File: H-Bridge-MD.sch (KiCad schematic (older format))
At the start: 80 parts, among them IC1 SI8650AB-B-IS1, IC2 A3921KLPTR-T, IC3 SI8650AB-B-IS1, IC4 A3921KLPTR-T, J1 PRT-10474, J2 Conn_01x02, J3 Conn_01x05, J4 PRT-10474, J5 Bus_PCIexpress_x16_164_Positi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, Q1 NVMFD5C650NLWFT1G, Q2 NVMFD5C650NLWFT1G, Q3 NVMFD5C650NLWFT1G, Q4 NVMFD5C650NLWFT1G, SW1 SW_Push, U1 LDO_3.3V, U2 STM32F042K6Tx, U3 MCP2562-E-SN

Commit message: Prototype1.2
Change: ST-LINK Conn, Rgs, Rg
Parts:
- removed R14, R15, R18, R19, R22, R23, R7, R8: 10K, Resistor_SMD:R_0603_1608Metric, symbol Device:R
- D6, D7: footprint Diode_SMD:D_2010_5025Metric -> Diode_SMD:D_0603_1608Metric
- R12, R13, R16, R17, R20, R21, R4, R5: value 100 -> 21
- R24, R27: value 30K -> 3K
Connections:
- wire segments 335 -> 295
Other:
- moved on the sheet: R12, R13, R16, R17, R20, R21, R4, R5

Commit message: Prototype1.3
Change LDO, 0.47uF size
Correction ST-LINK foot-print
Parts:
- removed U1: LDO_3.3V, Package_TO_SOT_SMD:TO-252-2, symbol Regulator_Linear:LF33_TO252
- added U1: LDL1117S33TR_SOT223-4, Package_TO_SOT_SMD:SOT-223-3_TabPin2, symbol Regulator_Linear:LD1117S33TR_SOT223
- C1: value 0.1uF -> 1uF
- C11, C17: footprint Capacitor_SMD:C_1206_3216Metric -> Capacitor_SMD:C_0805_2012Metric
- C2: value 0.1uF -> 4.7uF
- D1, D10, D11, D2, D3, D4, D5, D8, D9: footprint Diode_SMD:D_0603_1608Metric -> LED_SMD:LED_0603_1608Metric
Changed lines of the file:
@@
 Text GLabel 6050 7650 2    50   Output ~ 0
 MD_PWMH_1
-$Comp
-L Regulator_Linear:LF33_TO252 U1
-U 1 1 5DABB8B6
-P 1350 1650
-F 0 "U1" H 1200 1775 50  0000 C CNN
-F 1 "LDO_3.3V " H 1350 1775 50  0000 L CNN
-F 2 "Package_TO_SOT_SMD:TO-252-2" H 1350 1875 50  0001 C CIN
-F 3 "http://www.st.com/content/ccc/resource/technical/document/datasheet/c4/0e/7e/2a/be/bc/4c/bd/CD00000546.pdf/files/CD00000546.pdf/jcr:content/translations/en.CD00000546.pdf" H 1350 1600 50  0001 C CNN
-	1    1350 1650
-	1    0    0    -1
-$EndComp
 Wire Wire Line
 	7350 10500 7700 10500
@@
 P 1000 1800
 F 0 "C1" V 748 1800 50  0000 C CNN
-F 1 "0.1uF" V 839 1800 50  0000 C CNN
+F 1 "1uF" V 839 1800 50  0000 C CNN
 F 2 "Capacitor_SMD:C_0805_2012Metric" H 1038 1650 50  0001 C CNN
 F 3 "~" H 1000 1800 50  0001 C CNN
@@
 P 1700 1800
 F 0 "C2" V 1448 1800 50  0000 C CNN
-F 1 "0.1uF" V 1539 1800 50  0000 C CNN
+F 1 "4.7uF" V 1539 1800 50  0000 C CNN
 F 2 "Capacitor_SMD:C_0805_2012Metric" H 1738 1650 50  0001 C CNN
 F 3 "~" H 1700 1800 50  0001 C CNN
@@
 F 0 "D3" V 1339 2962 50  0000 C CNN
 F 1 "LED" V 1248 2962 50  0000 C CNN
-F 2 "Diode_SMD:D_0603_1608Metric" H 1300 3150 50  0001 C CNN
+F 2 "LED_SMD:LED_0603_1608Metric" H 1300 3150 50  0001 C CNN
 F 3 "~" H 1300 3150 50  0001 C CNN
 	1    1300 3150
@@
 F 0 "D2" V 1039 2962 50  0000 C CNN
 F 1 "LED" V 948 2962 50  0000 C CNN
-F 2 "Diode_SMD:D_0603_1608Metric" H 1000 3150 50  0001 C CNN
+F 2 "LED_SMD:LED_0603_1608Metric" H 1000 3150 50  0001 C CNN
 F 3 "~" H 1000 3150 50  0001 C CNN
 	1    1000 3150
@@
 F 0 "D1" V 739 3300 50  0000 C CNN
 F 1 "LED" V 648 3300 50  0000 C CNN
-F 2 "Diode_SMD:D_0603_1608Metric" H 700 3150 50  0001 C CNN
+F 2 "LED_SMD:LED_0603_1608Metric" H 700 3150 50  0001 C CNN
 F 3 "~" H 700 3150 50  0001 C CNN
 	1    700  3150
@@
 U 1 1 5E29BEB6
 P 7050 10250
-F 0 "C9" H 7165 10296 50  0000 L CNN
-F 1 "0.1uF" H 7165 10205 50  0000 L CNN
+F 0 "C9" H 7164 10204 50  0000 L CNN
+F 1 "0.1uF" H 7164 10295 50  0000 L CNN
 F 2 "Capacitor_SMD:C_0805_2012Metric" H 7088 10100 50  0001 C CNN
 F 3 "~" H 7050 10250 50  0001 C CNN
 	1    7050 10250
-	1    0    0    -1
+	-1   0    0    1
 $EndComp
 $Comp
@@
 U 1 1 5E2AD1D6
 P 7050 9750
-F 0 "C8" H 7165 9796 50  0000 L CNN
-F 1 "0.1uF" H 7165 9705 50  0000 L CNN
+F 0 "C8" H 6723 9796 50  0000 L CNN
+F 1 "0.1uF" H 6723 9705 50  0000 L CNN
 F 2 "Capacitor_SMD:C_0805_2012Metric" H 7088 9600 50  0001 C CNN
 F 3 "~" H 7050 9750 50  0001 C CNN
@@
 U 1 1 5E35AA28
 P 11250 6200
-F 0 "C14" H 11365 6246 50  0000 L CNN
-F 1 "0.1uF" H 11365 6155 50  0000 L CNN
+F 0 "C14" H 10923 6246 50  0000 L CNN
+F 1 "0.1uF" H 10923 6155 50  0000 L CNN
 F 2 "Capacitor_SMD:C_0805_2012Metric" H 11288 6050 50  0001 C CNN
 F 3 "~" H 11250 6200 50  0001 C CNN
@@
 U 1 1 5E36BC53
 P 11250 6700
-F 0 "C15" H 11365 6746 50  0000 L CNN
-F 1 "0.1uF" H 11365 6655 50  0000 L CNN
+F 0 "C15" H 10923 6746 50  0000 L CNN
+F 1 "0.1uF" H 10923 6655 50  0000 L CNN
 F 2 "Capacitor_SMD:C_0805_2012Metric" H 11288 6550 50  0001 C CNN
 F 3 "~" H 11250 6700 50  0001 C CNN
@@
 F 0 "C17" H 13174 7054 50  0000 L CNN
 F 1 "0.47uF" H 13174 7145 50  0000 L CNN
-F 2 "Capacitor_SMD:C_1206_3216Metric" H 13588 6950 50  0001 C CNN
+F 2 "Capacitor_SMD:C_0805_2012Metric" H 13588 6950 50  0001 C CNN
 F 3 "~" H 13550 7100 50  0001 C CNN
 	1    13550 7100
@@
 F 0 "C11" H 9465 10696 50  0000 L CNN
 F 1 "0.47uF" H 9465 10605 50  0000 L CNN
-F 2 "Capacitor_SMD:C_1206_3216Metric" H 9388 10500 50  0001 C CNN
+F 2 "Capacitor_SMD:C_0805_2012Metric" H 9388 10500 50  0001 C CNN
 F 3 "~" H 9350 10650 50  0001 C CNN
 	1    9350 10650
@@
 F 0 "D4" V 1639 2962 50  0000 C CNN
 F 1 "LED" V 1548 2962 50  0000 C CNN
-F 2 "Diode_SMD:D_0603_1608Metric" H 1600 3150 50  0001 C CNN
+F 2 "LED_SMD:LED_0603_1608Metric" H 1600 3150 50  0001 C CNN
 F 3 "~" H 1600 3150 50  0001 C CNN
 	1    1600 3150
@@
 F 0 "D5" V 2389 1033 50  0000 R CNN
 F 1 "LED" V 2298 1033 50  0000 R CNN
-F 2 "Diode_SMD:D_0603_1608Metric" H 2350 1150 50  0001 C CNN
+F 2 "LED_SMD:LED_0603_1608Metric" H 2350 1150 50  0001 C CNN
 F 3 "~" H 2350 1150 50  0001 C CNN
 	1    2350 1150
@@
 F 0 "D10" V 14239 8083 50  0000 R CNN
 F 1 "LED" V 14148 8083 50  0000 R CNN
-F 2 "Diode_SMD:D_0603_1608Metric" H 14200 8200 50  0001 C CNN
+F 2 "LED_SMD:LED_0603_1608Metric" H 14200 8200 50  0001 C CNN
 F 3 "~" H 14200 8200 50  0001 C CNN
 	1    14200 8200
@@
 F 0 "D11" V 14589 8083 50  0000 R CNN
 F 1 "LED" V 14498 8083 50  0000 R CNN
-F 2 "Diode_SMD:D_0603_1608Metric" H 14550 8200 50  0001 C CNN
+F 2 "LED_SMD:LED_0603_1608Metric" H 14550 8200 50  0001 C CNN
 F 3 "~" H 14550 8200 50  0001 C CNN
 	1    14550 8200
@@
 F 0 "D9" V 7989 8383 50  0000 R CNN
 F 1 "LED" V 7898 8383 50  0000 R CNN
-F 2 "Diode_SMD:D_0603_1608Metric" H 7950 8500 50  0001 C CNN
+F 2 "LED_SMD:LED_0603_1608Metric" H 7950 8500 50  0001 C CNN
 F 3 "~" H 7950 8500 50  0001 C CNN
 	1    7950 8500
@@
 F 0 "D8" V 7639 8383 50  0000 R CNN
 F 1 "LED" V 7548 8383 50  0000 R CNN
-F 2 "Diode_SMD:D_0603_1608Metric" H 7600 8500 50  0001 C CNN
+F 2 "LED_SMD:LED_0603_1608Metric" H 7600 8500 50  0001 C CNN
 F 3 "~" H 7600 8500 50  0001 C CNN
 	1    7600 8500
@@
 	4500 9700 4500 9500
 Connection ~ 4500 9500
+$Comp
+L Regulator_Linear:LD1117S33TR_SOT223 U1
+U 1 1 5DEBD597
+P 1350 1650
+F 0 "U1" H 1200 1775 50  0000 C CNN
+F 1 "LDL1117S33TR_SOT223-4" H 1350 1775 50  0000 L CNN
+F 2 "Package_TO_SOT_SMD:SOT-223-3_TabPin2" H 1350 1850 50  0001 C CNN
+F 3 "http://www.st.com/st-web-ui/static/active/en/resource/technical/document/datasheet/CD00000544.pdf" H 1450 1400 50  0001 C CNN
+	1    1350 1650
+	1    0    0    -1
+$EndComp
 $EndSCHEMATC

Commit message: update
軽微な配線の修正
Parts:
- removed J1, J4: PRT-10474, library:XT60PW-F_Reversible, symbol SamacSys_Parts:PRT-10474
- removed J2: Conn_01x02, Connector_JST:JST_XH_B2B-XH-A_1x02_P2.50mm_Vertical, symbol Connector_Generic:Conn_01x02
- removed J5: Bus_PCIexpress_x16_164_Position, library:BUS_PCIexpress_x16_164_Position, symbol SamacSys_Parts:Bus_PCIexpress_x16_164_Position
- removed R1, R2, R3, R6: 2.2K, Resistor_SMD:R_0603_1608Metric, symbol Device:R
- added J1, J4: Conn_01x02, XT60:XT60PW_Reversible, symbol Connector_Generic:Conn_01x02
- added J2: Conn_01x03, Connector_JST:JST_XH_B3B-XH-A_1x03_P2.50mm_Vertical, symbol Connector_Generic:Conn_01x03
- added J5: Bus_mechaken_PCIexpress_x16_164_Position, PCIe:BUS_mechaken_PCIexpress_x16_164_Position, symbol PCIe:Bus_mechaken_PCIexpress_x16_164_Position
- added RN1: R_Pack04, Resistor_SMD:R_Array_Concave_4x0603, symbol Device:R_Pack04
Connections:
- wire segments 295 -> 172
- no-connect marks 23 -> 15
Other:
- moved on the sheet: D1, D2, D3, D4

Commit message: remove RESET_SW
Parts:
- removed C3: 0.1uF, Capacitor_SMD:C_0805_2012Metric, symbol Device:C
- removed D5: LED, LED_SMD:LED_0603_1608Metric, symbol Device:LED
- removed Q1, Q2, Q3, Q4: NVMFD5C650NLWFT1G, SamacSys_Parts:NVMFD5C446NLWFT1G, symbol SamacSys_Parts:NVMFD5C650NLWFT1G
- removed R11, R9: 10K, Resistor_SMD:R_0603_1608Metric, symbol Device:R
- removed SW1: SW_Push, SamacSys_Parts:PTS647SM38SMTR2LFS, symbol Switch:SW_Push
- added Q1, Q2, Q3, Q4: NVMFD5C446NT1G, SamacSys_Parts:NVMFD5C446NLWFT1G, symbol SamacSys_Parts:NVMFD5C446NT1G
- J2: footprint Connector_JST:JST_XH_B3B-XH-A_1x03_P2.50mm_Vertical -> Connector_PinHeader_2.54mm:PinHeader_1x03_P2.54mm_Vertical
- J3: footprint Connector_JST:JST_XH_B5B-XH-A_1x05_P2.50mm_Vertical -> Connector_PinHeader_2.54mm:PinHeader_1x05_P2.54mm_Vertical
- U1: symbol Regulator_Linear:LD1117S33TR_SOT223 -> H-Bridge-MD-rescue:LD1117S33TR_SOT223-Regulator_Linear
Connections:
- net GNDPWR: now also Q2.1 (S1), Q2.3 (S2), Q3.1 (S1), Q3.3 (S2)
- net SA_0: now also Q3.6 (D1), Q4.1 (S1)
- net SA_1: now also Q1.1 (S1), Q2.6 (D1)
- net SB_0: now also Q3.5 (D2), Q4.3 (S2)
- net SB_1: now also Q1.3 (S2), Q2.5 (D2)
- net VCC: now also Q1.5 (D2), Q1.6 (D1), Q4.5 (D2), Q4.6 (D1)
- net at R12.2: now also Q2.2 (G1)
- net at R13.1: now also Q2.4 (G2)
- net at R4.2: now also Q1.2 (G1)
- net at R5.1: now also Q1.4 (G2)
- net at R16.2: now also Q3.2 (G1)
- net at R17.1: now also Q3.4 (G2)
- net at R20.2: now also Q4.2 (G1)
- net at R21.1: now also Q4.4 (G2)
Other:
- moved on the sheet: R20, R21

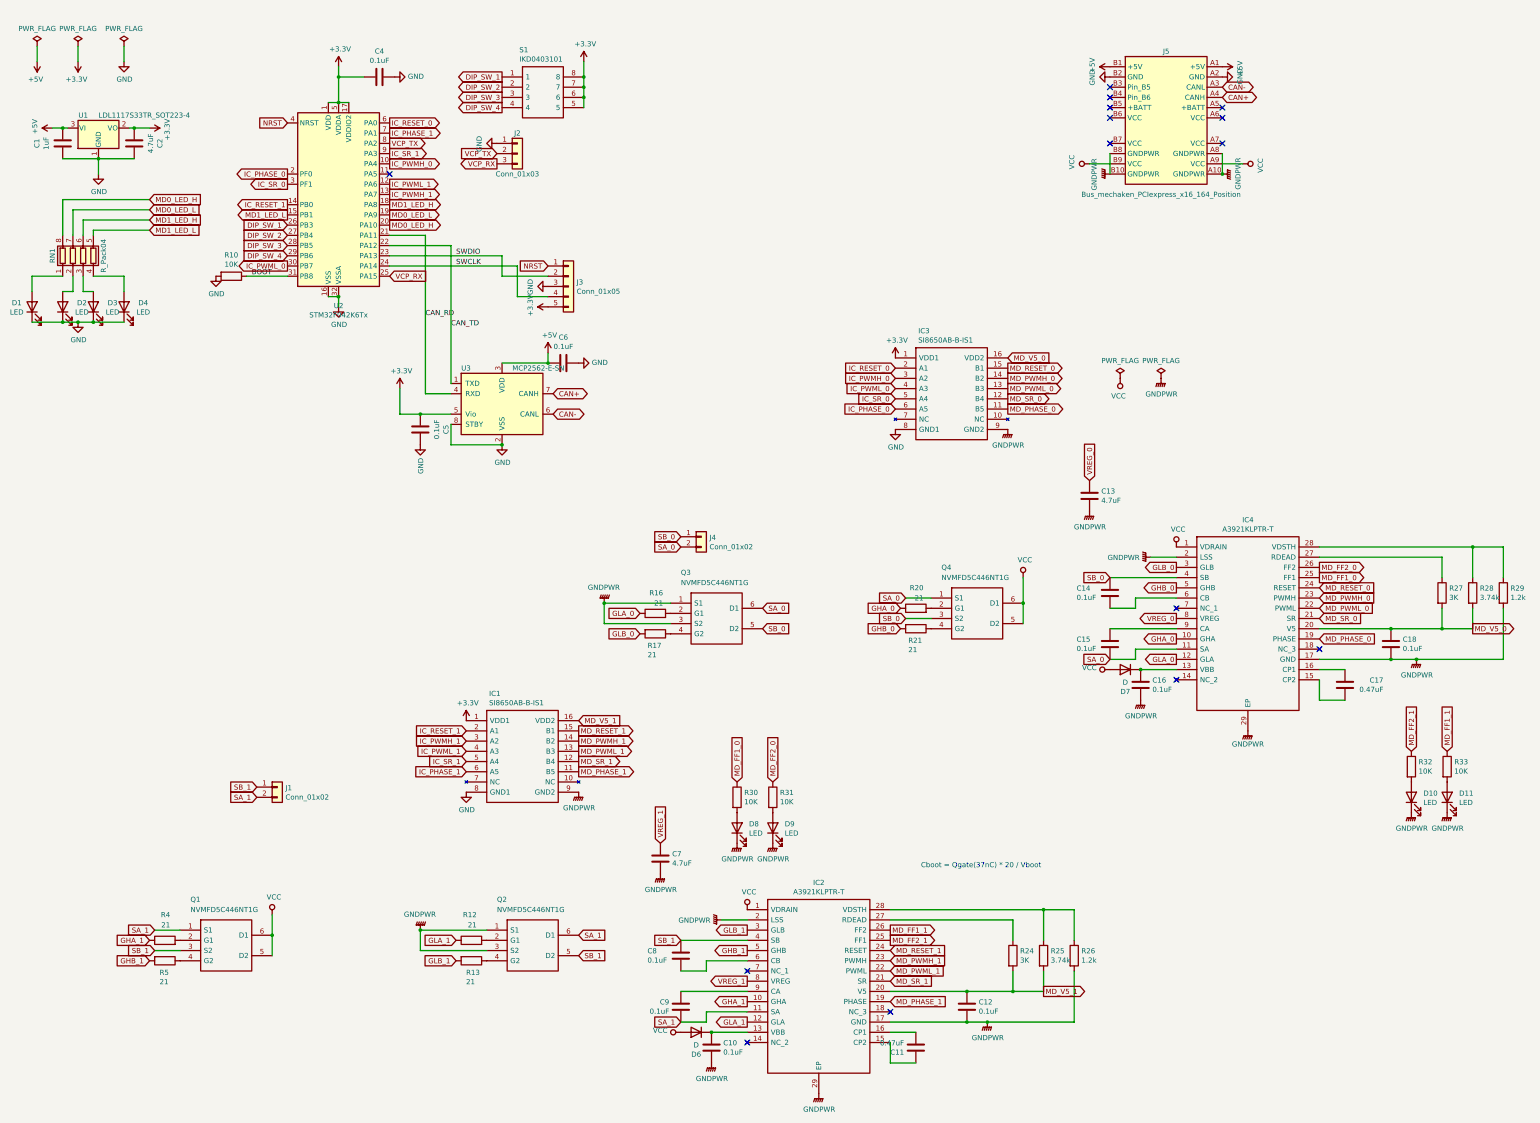
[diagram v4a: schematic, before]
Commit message: add 3V3LDO & pad
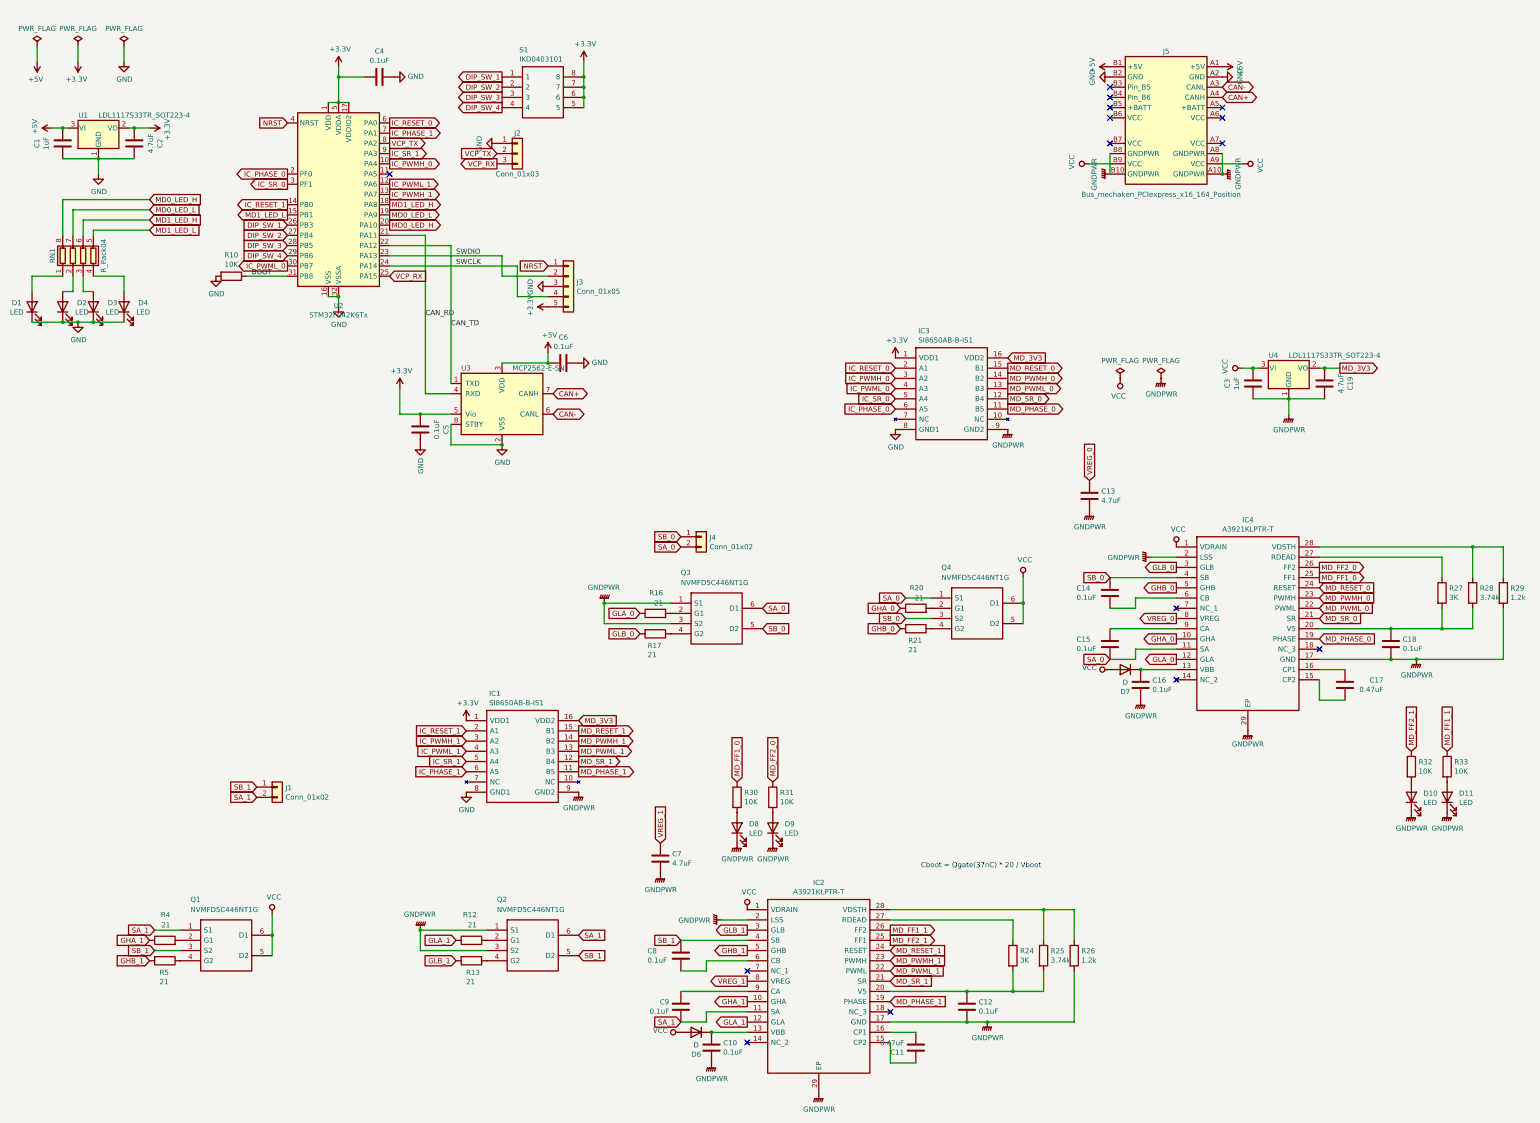
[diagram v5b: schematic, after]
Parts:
- added C19: 4.7uF, Capacitor_SMD:C_0805_2012Metric, symbol Device:C
- added C3: 1uF, Capacitor_SMD:C_0805_2012Metric, symbol Device:C
- added U4: LDL1117S33TR_SOT223-4, Package_TO_SOT_SMD:SOT-223-3_TabPin2, symbol H-Bridge-MD-rescue:LD1117S33TR_SOT223-Regulator_Linear
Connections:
- net GNDPWR: now also C19.1, C3.2, U4.1 (GND)
- net VCC: now also C3.1, U4.3 (VI)
- net MD_V5_0: no longer names the net of C18.1, IC4.20 (V5), R27.2, R28.2
- net MD_V5_0: no longer IC3.16 (VDD2)
- net MD_V5_1: no longer names the net of C12.1, IC2.20 (V5), R24.2, R25.2
- net MD_V5_1: no longer IC1.16 (VDD2)
- new net MD_3V3: C19.2, IC1.16 (VDD2), IC3.16 (VDD2), U4.2 (VO)
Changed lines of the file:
@@
 Wire Wire Line
 	7350 10500 7700 10500
-Wire Wire Line
-	9100 9400 10300 9400
-Wire Wire Line
-	9100 9300 10600 9300
-Wire Wire Line
-	10050 10400 10900 10400
 Connection ~ 10050 10400
-Wire Wire Line
-	10900 9900 10900 10400
-Connection ~ 10600 9300
-Wire Wire Line
-	10900 9300 10900 9600
-Wire Wire Line
-	10600 9300 10900 9300
-Wire Wire Line
-	10300 10100 10600 10100
-Connection ~ 10300 10100
-Wire Wire Line
-	10300 9400 10300 9600
-Wire Wire Line
-	10600 9300 10600 9600
-Wire Wire Line
-	10300 10100 10300 9900
-$Comp
-L Device:R R24
-U 1 1 5DA97CD1
-P 10300 9750
-F 0 "R24" H 10370 9796 50  0000 L CNN
-F 1 "3K" H 10370 9705 50  0000 L CNN
-F 2 "Resistor_SMD:R_0603_1608Metric" V 10230 9750 50  0001 C CNN
-F 3 "~" H 10300 9750 50  0001 C CNN
-	1    10300 9750
-	1    0    0    -1
-$EndComp
-Wire Wire Line
-	10600 9900 10600 10100
-$Comp
-L Device:R R26
-U 1 1 5DA97CC1
-P 10900 9750
-F 0 "R26" H 10970 9796 50  0000 L CNN
-F 1 "1.2k" H 10970 9705 50  0000 L CNN
-F 2 "Resistor_SMD:R_0603_1608Metric" V 10830 9750 50  0001 C CNN
-F 3 "~" H 10900 9750 50  0001 C CNN
-	1    10900 9750
-	1    0    0    -1
-$EndComp
-$Comp
-L Device:R R25
-U 1 1 5DA97CA9
-P 10600 9750
-F 0 "R25" H 10670 9796 50  0000 L CNN
-F 1 "3.74k" H 10670 9705 50  0000 L CNN
-F 2 "Resistor_SMD:R_0603_1608Metric" V 10530 9750 50  0001 C CNN
-F 3 "~" H 10600 9750 50  0001 C CNN
-	1    10600 9750
-	1    0    0    -1
-$EndComp
 $Comp
 L power:GNDPWR #PWR042
@@
 	1    0    0    -1
 $EndComp
-Connection ~ 9850 10100
-Wire Wire Line
-	9850 10100 10300 10100
 Connection ~ 9850 10400
 Wire Wire Line
 	9850 10400 10050 10400
-Wire Wire Line
-	9100 10100 9850 10100
 Wire Wire Line
 	9100 10400 9850 10400
@@
 Text GLabel 14200 7750 1    50   Input ~ 0
 MD_FF2_1
-Text GLabel 6050 7450 2    50   Input ~ 0
-MD_V5_1
-Text GLabel 10250 3900 2    50   Input ~ 0
-MD_V5_0
-Text GLabel 10600 10100 2    50   Output ~ 0
-MD_V5_1
-Text GLabel 14800 6550 2    50   Output ~ 0
-MD_V5_0
+Text GLabel 13500 4000 2    50   Output ~ 0
+MD_3V3
 Text Label 4800 3600 0    50   ~ 0
 CAN_TD
@@
 Wire Wire Line
 	10400 6300 10400 6500
+Wire Wire Line
+	12650 4000 12700 4000
+Connection ~ 12650 4000
+Wire Wire Line
+	13350 4000 13500 4000
+Connection ~ 13350 4000
+Wire Wire Line
+	13350 4300 13000 4300
+Wire Wire Line
+	13000 4300 12650 4300
+Connection ~ 13000 4300
+Wire Wire Line
+	13000 4300 13000 4450
+Wire Wire Line
+	13300 4000 13350 4000
+Wire Wire Line
+	12550 4000 12650 4000
+$Comp
+L Device:C C3
+U 1 1 5DF18189
+P 12650 4150
+F 0 "C3" V 12398 4150 50  0000 C CNN
+F 1 "1uF" V 12489 4150 50  0000 C CNN
+F 2 "Capacitor_SMD:C_0805_2012Metric" H 12688 4000 50  0001 C CNN
+F 3 "~" H 12650 4150 50  0001 C CNN
+	1    12650 4150
+	1    0    0    -1
+$EndComp
+$Comp
+L Device:C C19
+U 1 1 5DF1818F
+P 13350 4150
+F 0 "C19" V 13098 4150 50  0000 C CNN
+F 1 "4.7uF" V 13189 4150 50  0000 C CNN
+F 2 "Capacitor_SMD:C_0805_2012Metric" H 13388 4000 50  0001 C CNN
+F 3 "~" H 13350 4150 50  0001 C CNN
+	1    13350 4150
+	-1   0    0    1
+$EndComp
+$Comp
+L H-Bridge-MD-rescue:LD1117S33TR_SOT223-Regulator_Linear U4
+U 1 1 5DF181A7
+P 13000 4000
+F 0 "U4" H 12850 4125 50  0000 C CNN
+F 1 "LDL1117S33TR_SOT223-4" H 13000 4125 50  0000 L CNN
+F 2 "Package_TO_SOT_SMD:SOT-223-3_TabPin2" H 13000 4200 50  0001 C CNN
+F 3 "http://www.st.com/st-web-ui/static/active/en/resource/technical/document/datasheet/CD00000544.pdf" H 13100 3750 50  0001 C CNN
+	1    13000 4000
+	1    0    0    -1
+$EndComp
+$Comp
+L power:VCC #PWR0109
+U 1 1 5DF2B13A
+P 12550 4000
+F 0 "#PWR0109" H 12550 3850 50  0001 C CNN
+F 1 "VCC" H 12567 4173 50  0000 C CNN
+F 2 "" H 12550 4000 50  0001 C CNN
+F 3 "" H 12550 4000 50  0001 C CNN
+	1    12550 4000
+	0    -1   -1   0
+$EndComp
+Text GLabel 10250 3900 2    50   Input ~ 0
+MD_3V3
+Text GLabel 6050 7450 2    50   Input ~ 0
+MD_3V3
+Connection ~ 9850 10100
+Wire Wire Line
+	10050 10400 10900 10400
+Wire Wire Line
+	9100 10100 9850 10100
+Wire Wire Line
+	9850 10100 10300 10100
+$Comp
+L Device:R R25
+U 1 1 5DA97CA9
+P 10600 9750
+F 0 "R25" H 10670 9796 50  0000 L CNN
+F 1 "3.74k" H 10670 9705 50  0000 L CNN
+F 2 "Resistor_SMD:R_0603_1608Metric" V 10530 9750 50  0001 C CNN
+F 3 "~" H 10600 9750 50  0001 C CNN
+	1    10600 9750
+	1    0    0    -1
+$EndComp
+$Comp
+L Device:R R26
+U 1 1 5DA97CC1
+P 10900 9750
+F 0 "R26" H 10970 9796 50  0000 L CNN
+F 1 "1.2k" H 10970 9705 50  0000 L CNN
+F 2 "Resistor_SMD:R_0603_1608Metric" V 10830 9750 50  0001 C CNN
+F 3 "~" H 10900 9750 50  0001 C CNN
+	1    10900 9750
+	1    0    0    -1
+$EndComp
+Wire Wire Line
+	10600 9900 10600 10100
+$Comp
+L Device:R R24
+U 1 1 5DA97CD1
+P 10300 9750
+F 0 "R24" H 10370 9796 50  0000 L CNN
+F 1 "3K" H 10370 9705 50  0000 L CNN
+F 2 "Resistor_SMD:R_0603_1608Metric" V 10230 9750 50  0001 C CNN
+F 3 "~" H 10300 9750 50  0001 C CNN
+	1    10300 9750
+	1    0    0    -1
+$EndComp
+Wire Wire Line
+	10300 10100 10300 9900
+Wire Wire Line
+	10600 9300 10600 9600
+Wire Wire Line
+	10300 9400 10300 9600
+Connection ~ 10300 10100
+Wire Wire Line
+	10300 10100 10600 10100
+Wire Wire Line
+	10600 9300 10900 9300
+Wire Wire Line
+	10900 9300 10900 9600
+Connection ~ 10600 9300
+Wire Wire Line
+	10900 9900 10900 10400
+Wire Wire Line
+	9100 9300 10600 9300
+Wire Wire Line
+	9100 9400 10300 9400
+$Comp
+L power:GNDPWR #PWR?
+U 1 1 5DFADA6B
+P 13000 4450
+F 0 "#PWR?" H 13000 4250 50  0001 C CNN
+F 1 "GNDPWR" H 13004 4296 50  0000 C CNN
+F 2 "" H 13000 4400 50  0001 C CNN
+F 3 "" H 13000 4400 50  0001 C CNN
+	1    13000 4450
+	1    0    0    -1
+$EndComp
 $EndSCHEMATC

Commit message: Prototype 1.3
FusionPCB(12/12)
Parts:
- renumbered C11 to C10, C12 to C11, C13 to C12, C14 to C13, C15 to C14, C16 to C15, C3 to C16, C19 to C17, C17 to C18, C18 to C19, C4 to C3, C5 to C4, C6 to C5, C7 to C6, C8 to C7, C9 to C8, C10 to C9, D7 to D10, D6 to D5, D10 to D6, D11 to D7, R4 to R1, R30 to R10, R31 to R11, R20 to R12, R21 to R13, R24 to R14, R25 to R15, R26 to R16, R27 to R17, R28 to R18, R29 to R19, R5 to R2, R10 to R3, R12 to R4, R13 to R5, R16 to R6, R17 to R7, R32 to R8, R33 to R9
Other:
- moved on the sheet: D6, D7, D8, D9, R10, R11, R8, R9
